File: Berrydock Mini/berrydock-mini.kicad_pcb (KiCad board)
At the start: 2 copper layers, 50 x 50 mm, 86 parts, among them J1 RJ45, P1 CONN_01X16, P2 CONN_01X07, P3 CONN_01X04, P4 CONN_01X03, P5 USB_OTG, P6 USB_A, SW1 SWITCH_INV, SW2 BUTTON, U1 CP2102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

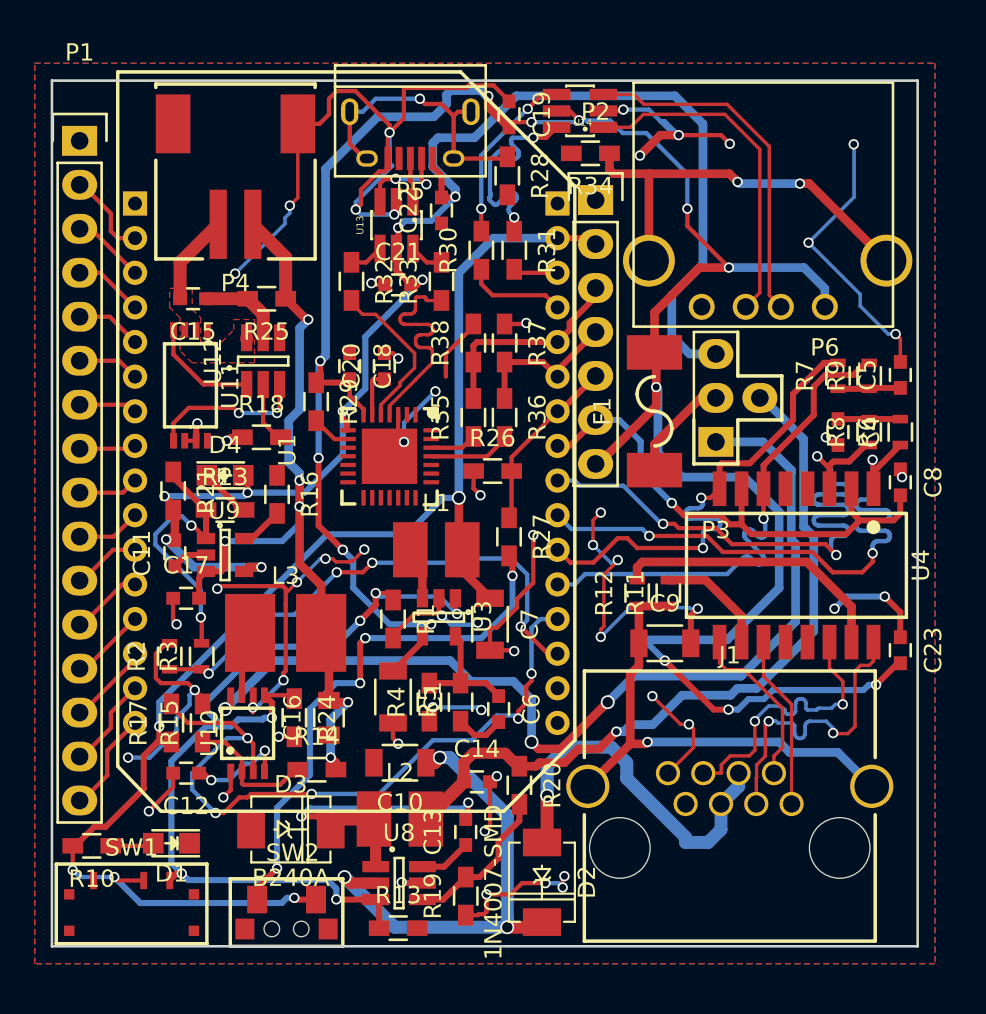
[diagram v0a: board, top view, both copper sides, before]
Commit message: changed all resistor footprints to 0603, added CE8301A50P component
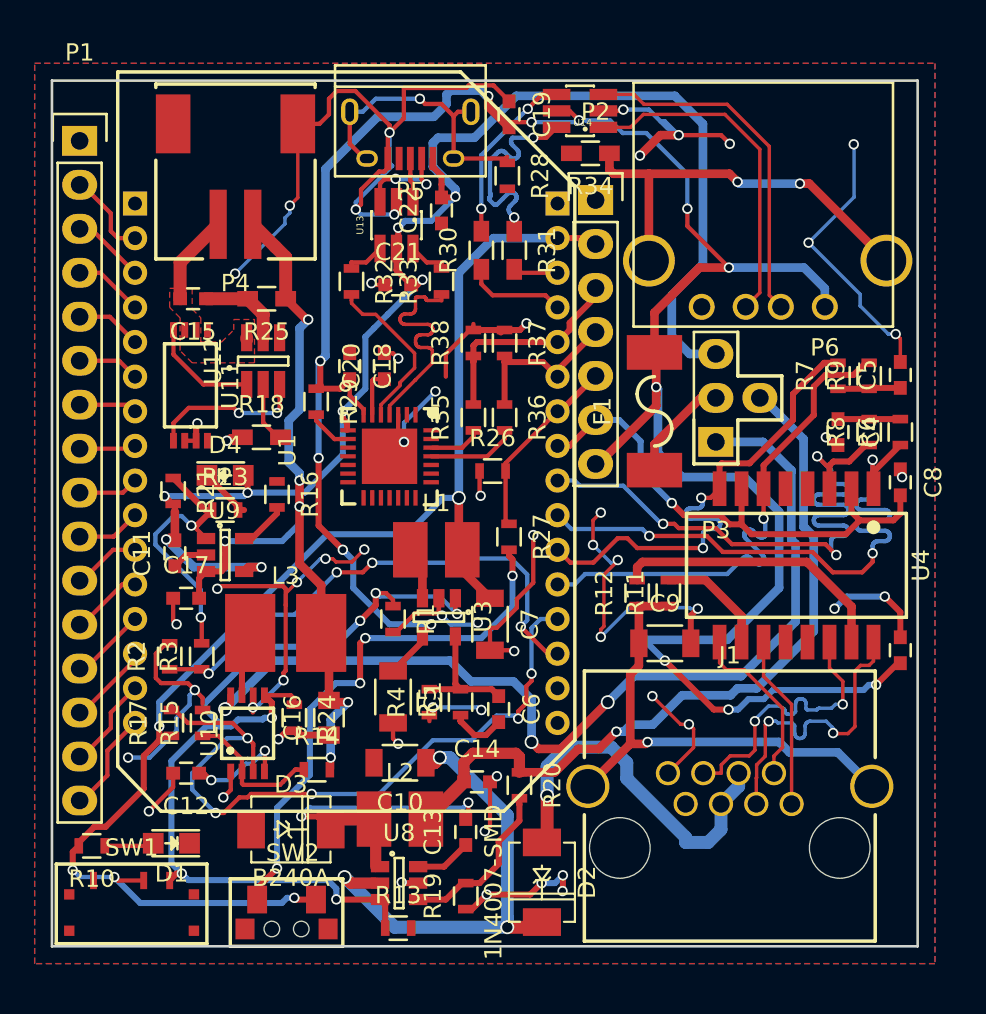
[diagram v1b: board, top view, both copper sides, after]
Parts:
- R1, R10, R13, R14, R15, R16, R17, R19, R20, R21, R23, R24, R26, R27, R28, R29, R32, R33, R35, R36, R37, R38, R4, R5: footprint Resistors_SMD:R_0603_HandSoldering -> Resistors_SMD:R_0603
- U8: footprint TO_SOT_Packages_SMD:SOT-23-6_Handsoldering -> TO_SOT_Packages_SMD:SOT-23-6
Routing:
- net GND: track 191.5 -> 194.9 mm
- net +5P: track 43.1 -> 43.9 mm
- net +5V: track 139.4 -> 140.2 mm
- net /PWRON: track 53.7 -> 54.4 mm
- net /TX0: track 9.00 -> 9.70 mm
- net /RX0: track 12.0 -> 12.7 mm
- net Net-(R14-Pad1): track 7.71 -> 8.35 mm
- net Net-(R19-Pad2): track 8.99 -> 9.55 mm
- net /FW_RST: track 10.4 -> 10.9 mm
